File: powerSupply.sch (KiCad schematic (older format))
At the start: 40 parts, among them U10 TPS7A4901, U11 LM3880, U12 TPS7A3001, U13 TPS7A3001, U8 TPS7A4901, U9 TPS7A4901

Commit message: Updated all part descriptions
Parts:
- C43, C52, C55, C62: Note 4μ7/25V X5R 0805 ceramic capacitor -> 4.7μF/25V X5R 0805 ceramic capacitor
- C44, C45, C53, C54, C56, C63: value 10u -> 10u/10V; Alt. Order Code (none) -> 81-GRM21BR61A106KE19; Alt. Supplier (none) -> Mouser; Note (none) -> 10μF/10V X5R 0805 ceramic capacitor; Package (none) -> 0805; Supplier (none) -> Farnell
- C46, C47, C48, C58, C59: Alt. Order Code (none) -> 77-VJ0603Y103KXACBC; Alt. Supplier (none) -> Mouser; Note (none) -> 10nF/100V X7R 0603 ceramic capacitor; Package (none) -> 0603; Supplier (none) -> Farnell
- C49, C50, C51, C60, C61: Alt. Order Code (none) -> 77-VJ0603Y103KXACBC; Alt. Supplier (none) -> Mouser; Note (none) -> 10 nF X7R 0603 ceramic capacitor; Package (none) -> 0603; Supplier (none) -> Farnell
- C57: value 1u -> 1u/10V; Alt. Order Code (none) -> 710-885012106010; Alt. Supplier (none) -> Mouser; Note (none) -> 1μF/10V X5R 0603 ceramic capacitor; Package (none) -> 0603; Supplier (none) -> Farnell
- R10, R11, R13, R15, R17, R18, R20, R22: Alt. Order Code (none) -> 667-ERJ-6ENF1202V; Alt. Supplier (none) -> Mouser; Note (none) -> 12kΩ/1% 0805 resistor; Package (none) -> 0805; Supplier (none) -> Farnell
- R12, R19: Alt. Order Code (none) -> 667-ERJ-6ENF1653V; Alt. Supplier (none) -> Mouser; Note (none) -> 165kΩ/1% 0805 resistor; Package (none) -> 0805; Supplier (none) -> Farnell
- R14, R21: Alt. Order Code (none) -> 667-ERJ-6ENF4872V; Alt. Supplier (none) -> Mouser; Note (none) -> 48.7kΩ/1% 0805 resistor; Package (none) -> 0805; Supplier (none) -> Farnell
- R16: value 48.7k -> 48k7; Alt. Order Code (none) -> 667-ERJ-6ENF4872V; Alt. Supplier (none) -> Mouser; Note (none) -> 48.7kΩ/1% 0805 resistor; Package (none) -> 0805; Supplier (none) -> Farnell
- U10, U8, U9: Alt. Order Code (none) -> 595-TPS7A4901DGNT; Alt. Supplier (none) -> Mouser; Note (none) -> Ultralow-noise positive linear regulator; Package (none) -> MSOP-8; Supplier (none) -> Farnell
- U11: Alt. Order Code (none) -> 926-LM3880MF1ABNOPB; Alt. Supplier (none) -> Mouser; Note (none) -> 3-output power sequencer; Package (none) -> SOT-23-6; Supplier (none) -> Farnell
- U12, U13: Alt. Order Code (none) -> 595-TPS7A3001DGNT; Alt. Supplier (none) -> Mouser; Note (none) -> Ultralow-noise negative linear regulator; Package (none) -> MSOP-8; Supplier (none) -> Farnell
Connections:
- wire segments 181 -> 142
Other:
- moved on the sheet: C44, C45, C56

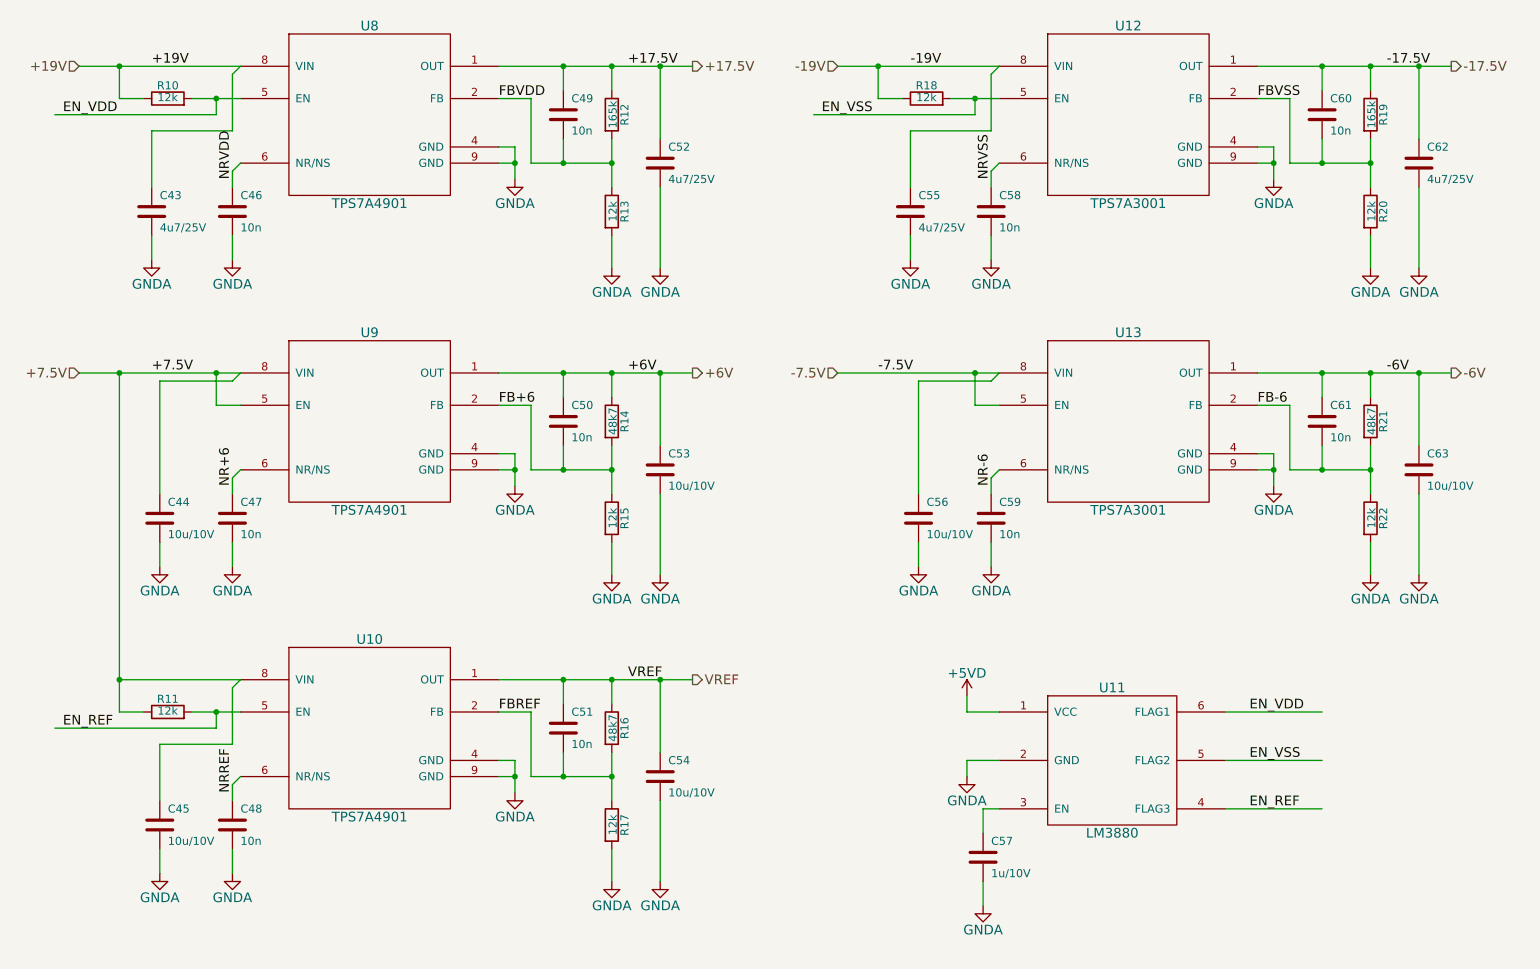
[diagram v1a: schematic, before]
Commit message: Fixed LM3880 pull-up resistors to 5V
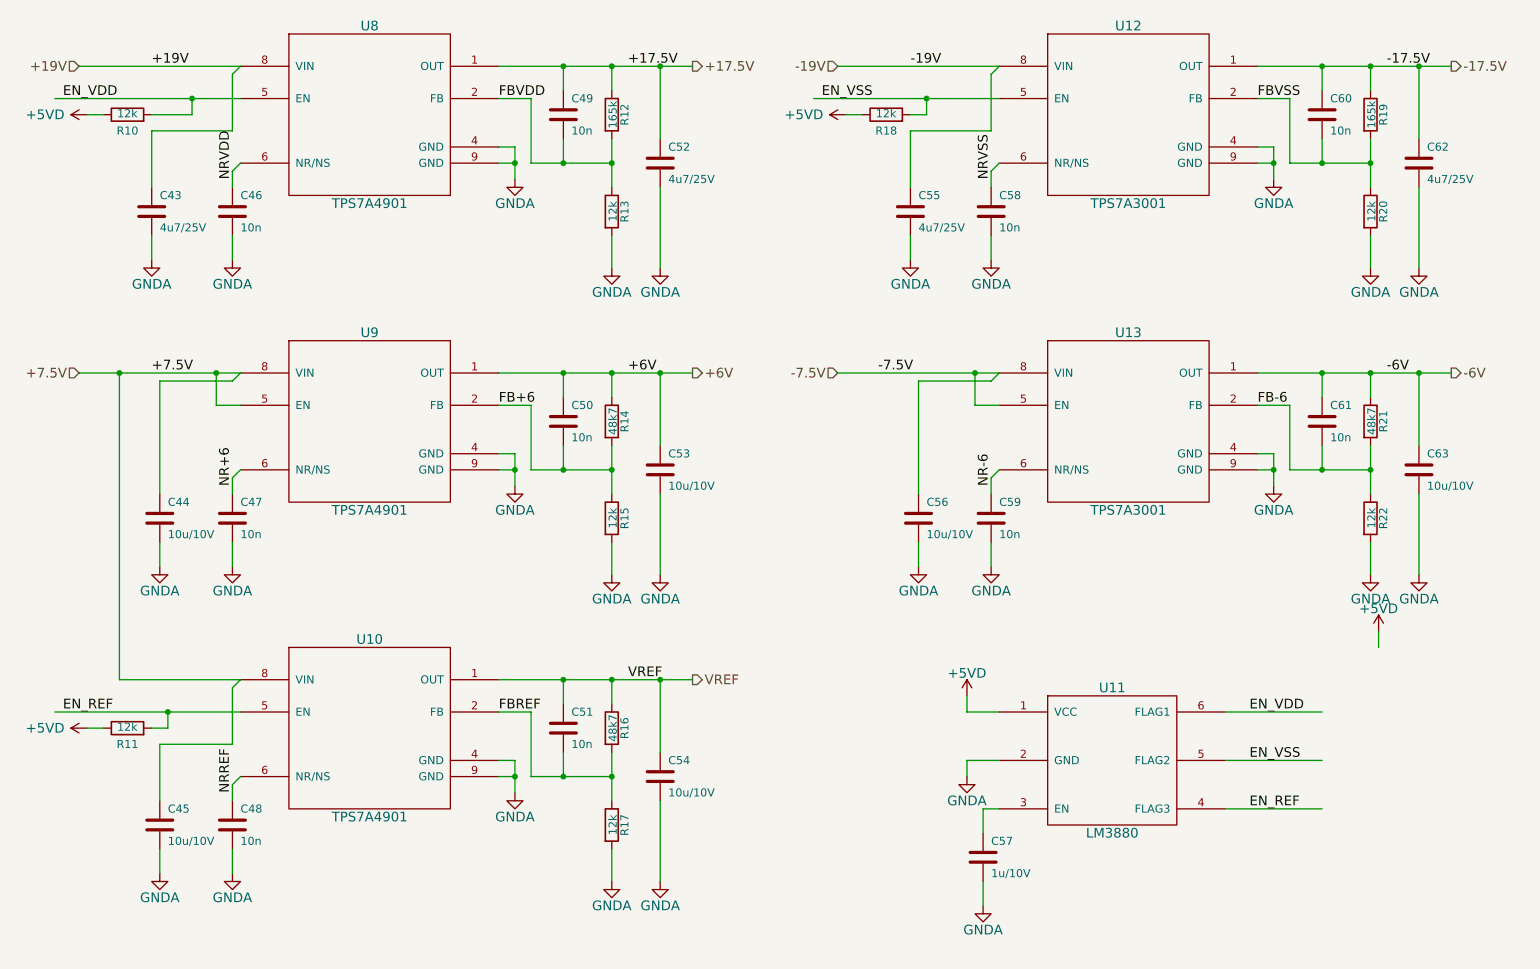
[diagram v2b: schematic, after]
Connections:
- wire segments 142 -> 141
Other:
- moved on the sheet: R10, R11, R18
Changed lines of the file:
@@
 L R R18
 U 1 1 5574013B
-P 7200 1200
-F 0 "R18" V 7280 1200 50  0000 C CNN
-F 1 "12k" V 7207 1201 50  0000 C CNN
-F 2 "Resistors_SMD:R_0805" V 7130 1200 30  0001 C CNN
-F 3 "" H 7200 1200 30  0000 C CNN
-F 4 "MCWR08X1202FTL" V 7200 1200 60  0001 C CNN "Part Number"
-F 5 "Multicomp" V 7200 1200 60  0001 C CNN "Manufacturer"
-F 6 "0805" H 7200 1200 60  0001 C CNN "Package"
-F 7 "Farnell" H 7200 1200 60  0001 C CNN "Supplier"
-F 8 "2447563" V 7200 1200 60  0001 C CNN "Order Code"
-F 9 "Mouser" H 7200 1200 60  0001 C CNN "Alt. Supplier"
-F 10 "667-ERJ-6ENF1202V" H 7200 1200 60  0001 C CNN "Alt. Order Code"
-F 11 "12kΩ/1% 0805 resistor" H 7200 1200 60  0001 C CNN "Note"
-	1    7200 1200
+P 6950 1300
+F 0 "R18" V 6850 1300 50  0000 C CNN
+F 1 "12k" V 6957 1301 50  0000 C CNN
+F 2 "Resistors_SMD:R_0805" V 6880 1300 30  0001 C CNN
+F 3 "" H 6950 1300 30  0000 C CNN
+F 4 "MCWR08X1202FTL" V 6950 1300 60  0001 C CNN "Part Number"
+F 5 "Multicomp" V 6950 1300 60  0001 C CNN "Manufacturer"
+F 6 "0805" H 6950 1300 60  0001 C CNN "Package"
+F 7 "Farnell" H 6950 1300 60  0001 C CNN "Supplier"
+F 8 "2447563" V 6950 1300 60  0001 C CNN "Order Code"
+F 9 "Mouser" H 6950 1300 60  0001 C CNN "Alt. Supplier"
+F 10 "667-ERJ-6ENF1202V" H 6950 1300 60  0001 C CNN "Alt. Order Code"
+F 11 "12kΩ/1% 0805 resistor" H 6950 1300 60  0001 C CNN "Note"
+	1    6950 1300
 	0    -1   -1   0
 $EndComp
-Text Label 6550 1300 0    60   ~ 0
+Text Label 6550 1200 0    60   ~ 0
 EN_VSS
 $Comp
 L R R10
 U 1 1 55740E12
-P 2500 1200
-F 0 "R10" V 2580 1200 50  0000 C CNN
-F 1 "12k" V 2507 1201 50  0000 C CNN
-F 2 "Resistors_SMD:R_0805" V 2430 1200 30  0001 C CNN
-F 3 "" H 2500 1200 30  0000 C CNN
-F 4 "MCWR08X1202FTL" V 2500 1200 60  0001 C CNN "Part Number"
-F 5 "Multicomp" V 2500 1200 60  0001 C CNN "Manufacturer"
-F 6 "0805" H 2500 1200 60  0001 C CNN "Package"
-F 7 "Farnell" H 2500 1200 60  0001 C CNN "Supplier"
-F 8 "2447563" V 2500 1200 60  0001 C CNN "Order Code"
-F 9 "Mouser" H 2500 1200 60  0001 C CNN "Alt. Supplier"
-F 10 "667-ERJ-6ENF1202V" H 2500 1200 60  0001 C CNN "Alt. Order Code"
-F 11 "12kΩ/1% 0805 resistor" H 2500 1200 60  0001 C CNN "Note"
-	1    2500 1200
+P 2250 1300
+F 0 "R10" V 2150 1300 50  0000 C CNN
+F 1 "12k" V 2257 1301 50  0000 C CNN
+F 2 "Resistors_SMD:R_0805" V 2180 1300 30  0001 C CNN
+F 3 "" H 2250 1300 30  0000 C CNN
+F 4 "MCWR08X1202FTL" V 2250 1300 60  0001 C CNN "Part Number"
+F 5 "Multicomp" V 2250 1300 60  0001 C CNN "Manufacturer"
+F 6 "0805" H 2250 1300 60  0001 C CNN "Package"
+F 7 "Farnell" H 2250 1300 60  0001 C CNN "Supplier"
+F 8 "2447563" V 2250 1300 60  0001 C CNN "Order Code"
+F 9 "Mouser" H 2250 1300 60  0001 C CNN "Alt. Supplier"
+F 10 "667-ERJ-6ENF1202V" H 2250 1300 60  0001 C CNN "Alt. Order Code"
+F 11 "12kΩ/1% 0805 resistor" H 2250 1300 60  0001 C CNN "Note"
+	1    2250 1300
 	0    -1   -1   0
 $EndComp
-Text Label 1850 1300 0    60   ~ 0
+Text Label 1850 1200 0    60   ~ 0
 EN_VDD
 $Comp
 L R R11
 U 1 1 55742790
-P 2500 5000
-F 0 "R11" V 2580 5000 50  0000 C CNN
-F 1 "12k" V 2507 5001 50  0000 C CNN
-F 2 "Resistors_SMD:R_0805" V 2430 5000 30  0001 C CNN
-F 3 "" H 2500 5000 30  0000 C CNN
-F 4 "MCWR08X1202FTL" V 2500 5000 60  0001 C CNN "Part Number"
-F 5 "Multicomp" V 2500 5000 60  0001 C CNN "Manufacturer"
-F 6 "0805" H 2500 5000 60  0001 C CNN "Package"
-F 7 "Farnell" H 2500 5000 60  0001 C CNN "Supplier"
-F 8 "2447563" V 2500 5000 60  0001 C CNN "Order Code"
-F 9 "Mouser" H 2500 5000 60  0001 C CNN "Alt. Supplier"
-F 10 "667-ERJ-6ENF1202V" H 2500 5000 60  0001 C CNN "Alt. Order Code"
-F 11 "12kΩ/1% 0805 resistor" H 2500 5000 60  0001 C CNN "Note"
-	1    2500 5000
+P 2250 5100
+F 0 "R11" V 2150 5100 50  0000 C CNN
+F 1 "12k" V 2257 5101 50  0000 C CNN
+F 2 "Resistors_SMD:R_0805" V 2180 5100 30  0001 C CNN
+F 3 "" H 2250 5100 30  0000 C CNN
+F 4 "MCWR08X1202FTL" V 2250 5100 60  0001 C CNN "Part Number"
+F 5 "Multicomp" V 2250 5100 60  0001 C CNN "Manufacturer"
+F 6 "0805" H 2250 5100 60  0001 C CNN "Package"
+F 7 "Farnell" H 2250 5100 60  0001 C CNN "Supplier"
+F 8 "2447563" V 2250 5100 60  0001 C CNN "Order Code"
+F 9 "Mouser" H 2250 5100 60  0001 C CNN "Alt. Supplier"
+F 10 "667-ERJ-6ENF1202V" H 2250 5100 60  0001 C CNN "Alt. Order Code"
+F 11 "12kΩ/1% 0805 resistor" H 2250 5100 60  0001 C CNN "Note"
+	1    2250 5100
 	0    -1   -1   0
 $EndComp
-Text Label 1850 5100 0    60   ~ 0
+Text Label 1850 5000 0    60   ~ 0
 EN_REF
 Wire Wire Line
@@
 Connection ~ 7500 2900
 Wire Wire Line
-	7350 1200 7650 1200
-Wire Wire Line
 	7600 1050 7600 1400
 Wire Wire Line
@@
 	7100 1400 7100 1750
 Wire Wire Line
-	7050 1200 6900 1200
-Wire Wire Line
-	6900 1200 6900 1000
-Connection ~ 6900 1000
-Wire Wire Line
-	7500 1200 7500 1300
-Wire Wire Line
-	7500 1300 6500 1300
-Connection ~ 7500 1200
+	6500 1200 7650 1200
 Wire Wire Line
 	2900 1050 2900 1400
@@
 	2400 1400 2400 1750
 Wire Wire Line
-	2650 1200 2950 1200
-Wire Wire Line
-	2800 1200 2800 1300
-Wire Wire Line
-	2800 1300 1800 1300
-Connection ~ 2800 1200
-Wire Wire Line
-	2200 1000 2200 1200
-Wire Wire Line
-	2200 1200 2350 1200
-Connection ~ 2200 1000
+	1800 1200 2950 1200
+Connection ~ 2650 1200
 Wire Wire Line
 	2900 4850 2900 5200
@@
 	2900 5200 2450 5200
 Wire Wire Line
-	2650 5000 2950 5000
-Wire Wire Line
-	2800 5000 2800 5100
-Wire Wire Line
-	2800 5100 1800 5100
-Connection ~ 2800 5000
-Wire Wire Line
-	2200 5000 2350 5000
-Wire Wire Line
-	2200 2900 2200 5000
-Connection ~ 2200 4800
+	2500 5100 2500 5000
+Wire Wire Line
+	1800 5000 2950 5000
+Connection ~ 2500 5000
+Wire Wire Line
+	2200 2900 2200 4800
 Wire Wire Line
 	5550 1000 5550 1450
@@
 Connection ~ 2200 2900
 Wire Wire Line
-	2950 4800 2200 4800
+	2200 4800 2950 4800
 $Comp
 L GNDA #PWR081
@@
 	1    0    0    -1
 $EndComp
+Wire Wire Line
+	10000 4600 10000 4500
+$Comp
+L +5VD #PWR083
+U 1 1 56D84E64
+P 10000 4500
+F 0 "#PWR083" H 10000 4350 60  0001 C CNN
+F 1 "+5VD" H 10000 4640 60  0000 C CNN
+F 2 "" H 10000 4500 60  0000 C CNN
+F 3 "" H 10000 4500 60  0000 C CNN
+	1    10000 4500
+	1    0    0    -1
+$EndComp
+Wire Wire Line
+	7100 1300 7200 1300
+Wire Wire Line
+	7200 1300 7200 1200
+Connection ~ 7200 1200
+$Comp
+L +5VD #PWR084
+U 1 1 56D88685
+P 6700 1300
+F 0 "#PWR084" H 6700 1150 60  0001 C CNN
+F 1 "+5VD" V 6700 1440 60  0000 L CNN
+F 2 "" H 6700 1300 60  0000 C CNN
+F 3 "" H 6700 1300 60  0000 C CNN
+	1    6700 1300
+	0    -1   -1   0
+$EndComp
+Wire Wire Line
+	6800 1300 6700 1300
+$Comp
+L +5VD #PWR085
+U 1 1 56D89B26
+P 2000 5100
+F 0 "#PWR085" H 2000 4950 60  0001 C CNN
+F 1 "+5VD" V 2000 5240 60  0000 L CNN
+F 2 "" H 2000 5100 60  0000 C CNN
+F 3 "" H 2000 5100 60  0000 C CNN
+	1    2000 5100
+	0    -1   -1   0
+$EndComp
+Wire Wire Line
+	2100 5100 2000 5100
+Wire Wire Line
+	2400 5100 2500 5100
+$Comp
+L +5VD #PWR086
+U 1 1 56D8B815
+P 2000 1300
+F 0 "#PWR086" H 2000 1150 60  0001 C CNN
+F 1 "+5VD" V 2000 1440 60  0000 L CNN
+F 2 "" H 2000 1300 60  0000 C CNN
+F 3 "" H 2000 1300 60  0000 C CNN
+	1    2000 1300
+	0    -1   -1   0
+$EndComp
+Wire Wire Line
+	2100 1300 2000 1300
+Wire Wire Line
+	2650 1200 2650 1300
+Wire Wire Line
+	2650 1300 2400 1300
 $EndSCHEMATC

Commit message: Fixed ground problems, added bypass capacitors, added resistor between digital isolator and DAC
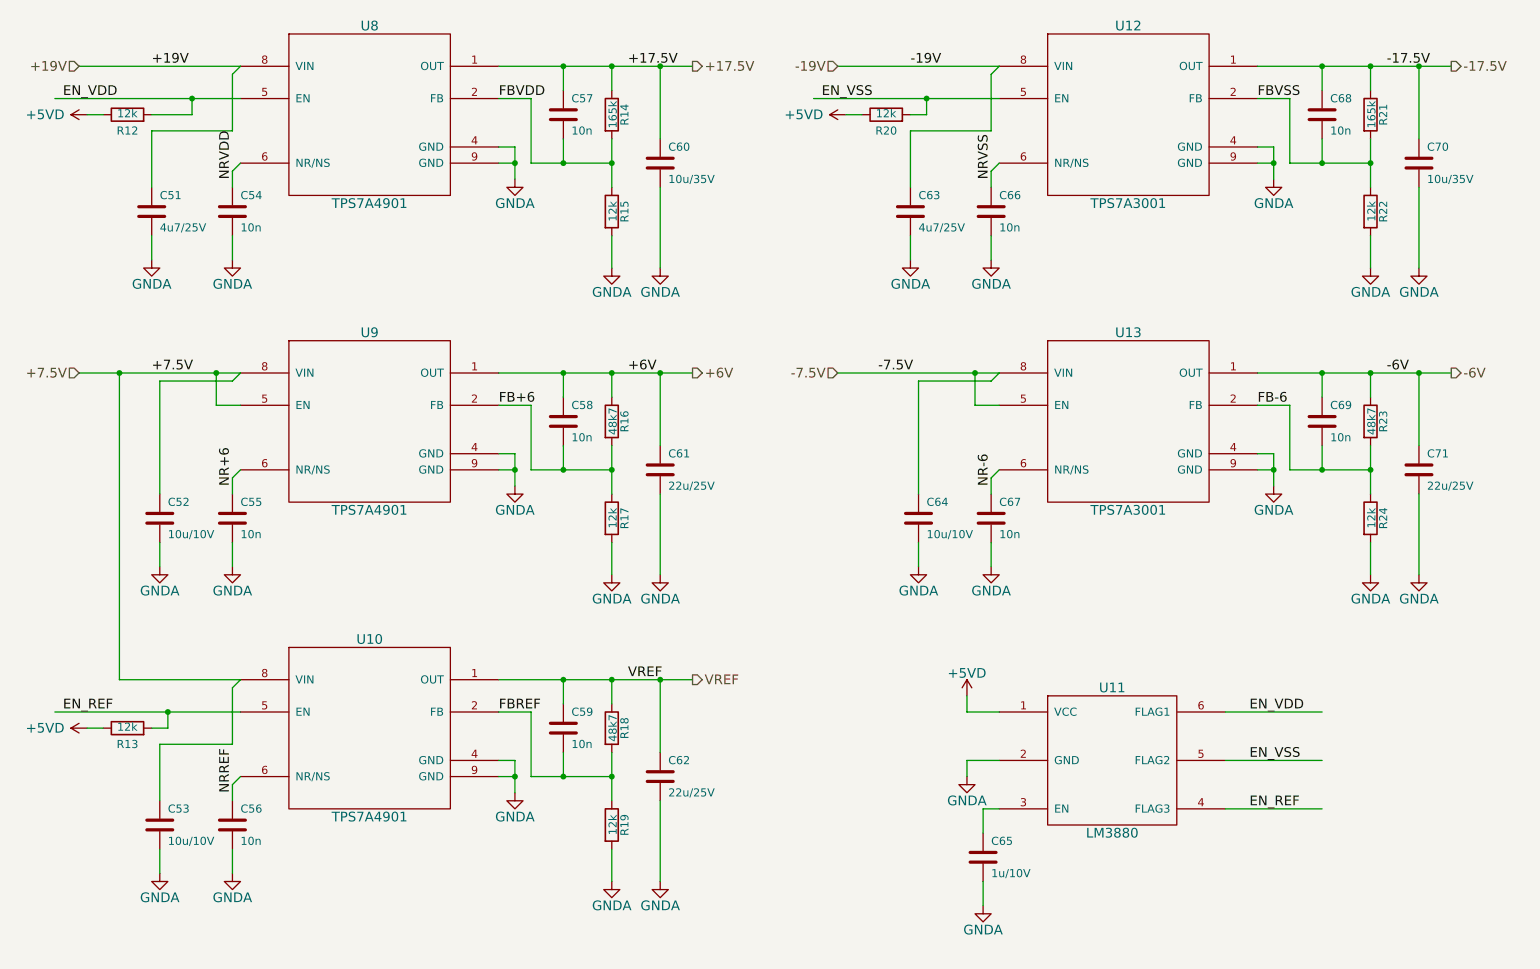
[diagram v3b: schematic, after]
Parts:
- removed C52: 4u7/25V, Capacitors_SMD:C_0805, symbol C
- removed C54, C63: 10u/10V, Capacitors_SMD:C_0805, symbol C
- added C60: 10u/35V, Capacitors_SMD:C_1210, symbol C
- added C62, C71: 22u/25V, Capacitors_SMD:C_1210, symbol C
- C61: renamed from C53; value 10u/10V -> 22u/25V; footprint Capacitors_SMD:C_0805 -> Capacitors_SMD:C_1210; Alt. Order Code 81-GRM21BR61A106KE19 -> 81-GRM32ER61E226ME5L; Note 10μF/10V X5R 0805 ceramic capacitor -> 22μF/25V X5R 1210 ceramic capacitor; Order Code 1828805 -> 1735539; Package 0805 -> 1210; Part Number GRM21BR61A106KE19L -> GRM32ER61E226ME15L
- C70: renamed from C62; value 4u7/25V -> 10u/35V; footprint Capacitors_SMD:C_0805 -> Capacitors_SMD:C_1210; Alt. Order Code 81-GRM21BR61E475MA2L -> 81-GRM32ER6YA106KA2L; Note 4.7μF/25V X5R 0805 ceramic capacitor -> 10μF/35V X5R 1210 ceramic capacitor; Order Code 1735529 -> 1845763; Package 0805 -> 1210; Part Number GRM21BR61E475MA12L -> GRM32ER6YA106KA12L
- renumbered C43 to C51, C44 to C52, C45 to C53, C46 to C54, C47 to C55, C48 to C56, C49 to C57, C50 to C58, C51 to C59, C55 to C63, C56 to C64, C57 to C65, C58 to C66, C59 to C67, C60 to C68, C61 to C69, R10 to R12, R11 to R13, R12 to R14, R13 to R15, R14 to R16, R15 to R17, R16 to R18, R17 to R19, R18 to R20, R19 to R21, R20 to R22, R21 to R23, R22 to R24
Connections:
- wire segments 141 -> 140

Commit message: Fixed SMA connector labels and 4u7/25V capacitor order code
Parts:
- C51, C63: Order Code 1735529 -> 2362111
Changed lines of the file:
@@
 F 6 "0805" H 2400 1900 60  0001 C CNN "Package"
 F 7 "Farnell" H 2400 1900 60  0001 C CNN "Supplier"
-F 8 "1735529" H 2400 1900 60  0001 C CNN "Order Code"
+F 8 "2362111" H 2400 1900 60  0001 C CNN "Order Code"
 F 9 "Mouser" H 2400 1900 60  0001 C CNN "Alt. Supplier"
 F 10 "81-GRM21BR61E475MA2L" H 2400 1900 60  0001 C CNN "Alt. Order Code"
@@
 F 6 "0805" H 7100 1900 60  0001 C CNN "Package"
 F 7 "Farnell" H 7100 1900 60  0001 C CNN "Supplier"
-F 8 "1735529" H 7100 1900 60  0001 C CNN "Order Code"
+F 8 "2362111" H 7100 1900 60  0001 C CNN "Order Code"
 F 9 "Mouser" H 7100 1900 60  0001 C CNN "Alt. Supplier"
 F 10 "81-GRM21BR61E475MA2L" H 7100 1900 60  0001 C CNN "Alt. Order Code"
